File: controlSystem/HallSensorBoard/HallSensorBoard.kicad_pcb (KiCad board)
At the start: 2 copper layers, 12.7 x 16.8 mm, 5 parts, among them J1 22-23-2031, U1 DRV5056-Q1

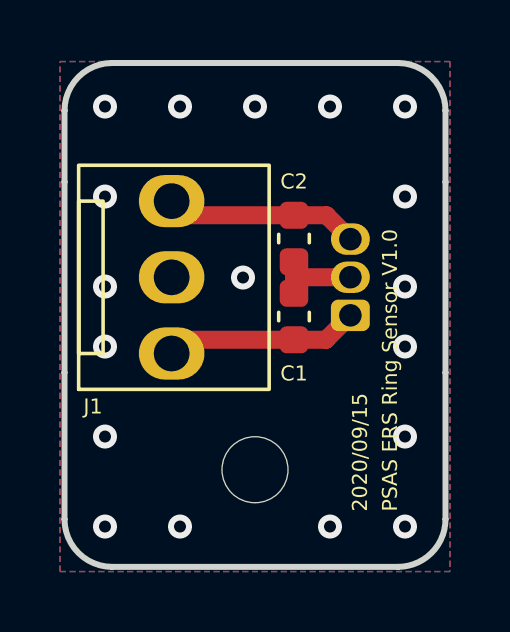
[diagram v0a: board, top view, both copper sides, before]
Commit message: Added ERS hall effect sensor board and spring pin boards
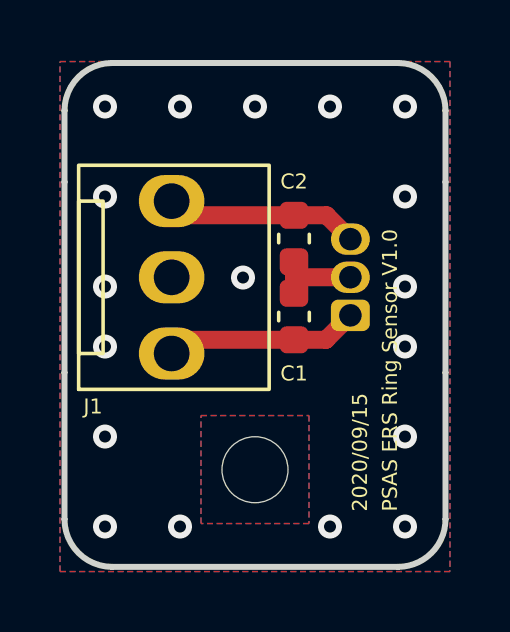
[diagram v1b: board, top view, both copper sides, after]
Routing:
- added copper zone on B.Cu, net Net-(J1-Pad3)
- added copper zone on F.Cu, net Net-(J1-Pad3)
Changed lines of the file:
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@@
+    )
+  )
+  (zone (net 3) (net_name "Net-(J1-Pad3)") (layers F&B.Cu) (hatch edge 0.508)
+    (priority 2)
+    (connect_pads (clearance 0.254))
+    (min_thickness 0.254) (filled_areas_thickness no)
+    (fill yes (thermal_gap 0.508) (thermal_bridge_width 0.508) (smoothing fillet) (radius 3))
+    (polygon
+      (pts
+        (xy 156.8 108.4)
+        (xy 153.2 108.4)
+        (xy 153.2 104.8)
+        (xy 156.8 104.8)
+      )
     )
   )
